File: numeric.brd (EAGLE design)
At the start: 93.3 x 42.5 mm, 28 parts, among them IC1 MEGA8-AI, Q2 BC817-16SMD, Q3 BC817-16SMD, SW2 EC12E_SW

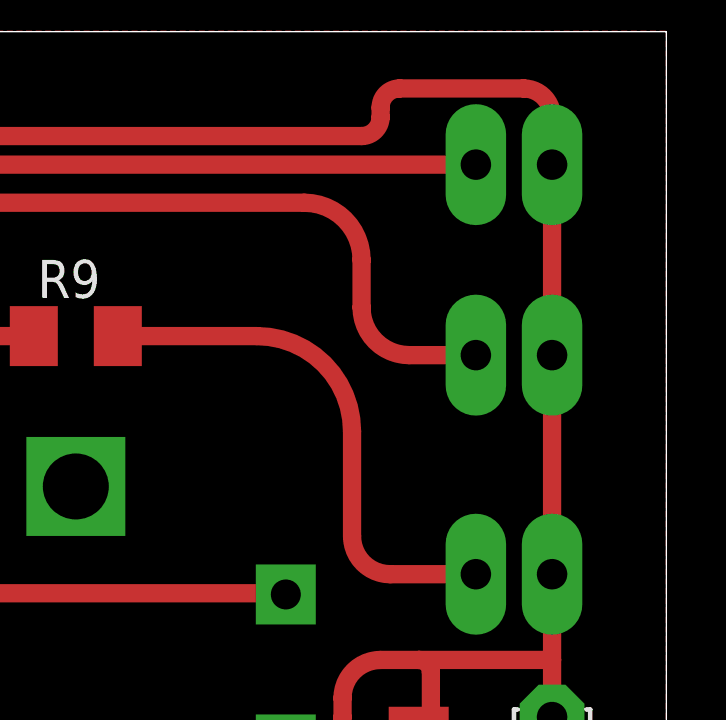
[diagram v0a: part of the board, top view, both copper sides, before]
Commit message: Переразвел 2горячую" плату - уменьшил длинну упарвляющей дорожки, увеличил ширину силовых дорожек. Под тиристором уменьшились зазоры - на перетрав, при необходимости - доработать напильником %) Добавил подписи "+" на разъемах
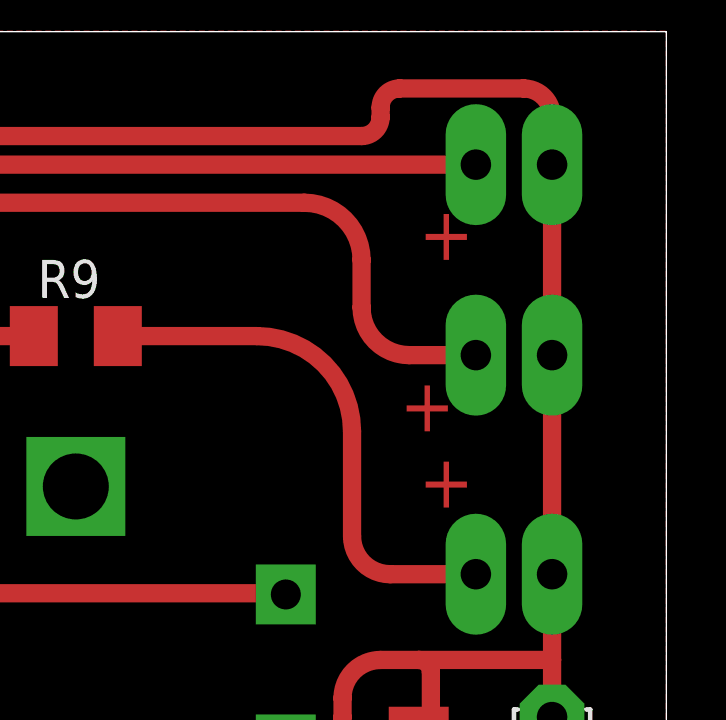
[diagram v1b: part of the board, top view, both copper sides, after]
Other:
- board text added: "+"
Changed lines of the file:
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@@
 <circle x="3.81" y="38.735" radius="1.905" width="0.4064" layer="1"/>
 <circle x="88.9" y="4.445" radius="1.905" width="0.4064" layer="1"/>
+<text x="85.09" y="26.67" size="1.778" layer="1">+</text>
+<text x="84.455" y="29.21" size="1.778" layer="1">+</text>
+<text x="85.09" y="34.925" size="1.778" layer="1">+</text>
 </plain>
 <attributes>
